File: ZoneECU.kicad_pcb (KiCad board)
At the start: 4 copper layers, 70.5 x 76.3 mm, 85 parts, among them J1 5007620481, J2 Conn_02x03_Odd_Even, SW1 SW_Push, U1 STM32F103RBTx, U2 SN65HVD234, U3 LMR50410, U4 LMR50410, U5 MAX3221, U7 DRV8871DDA, U9 SN74LVC4245A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

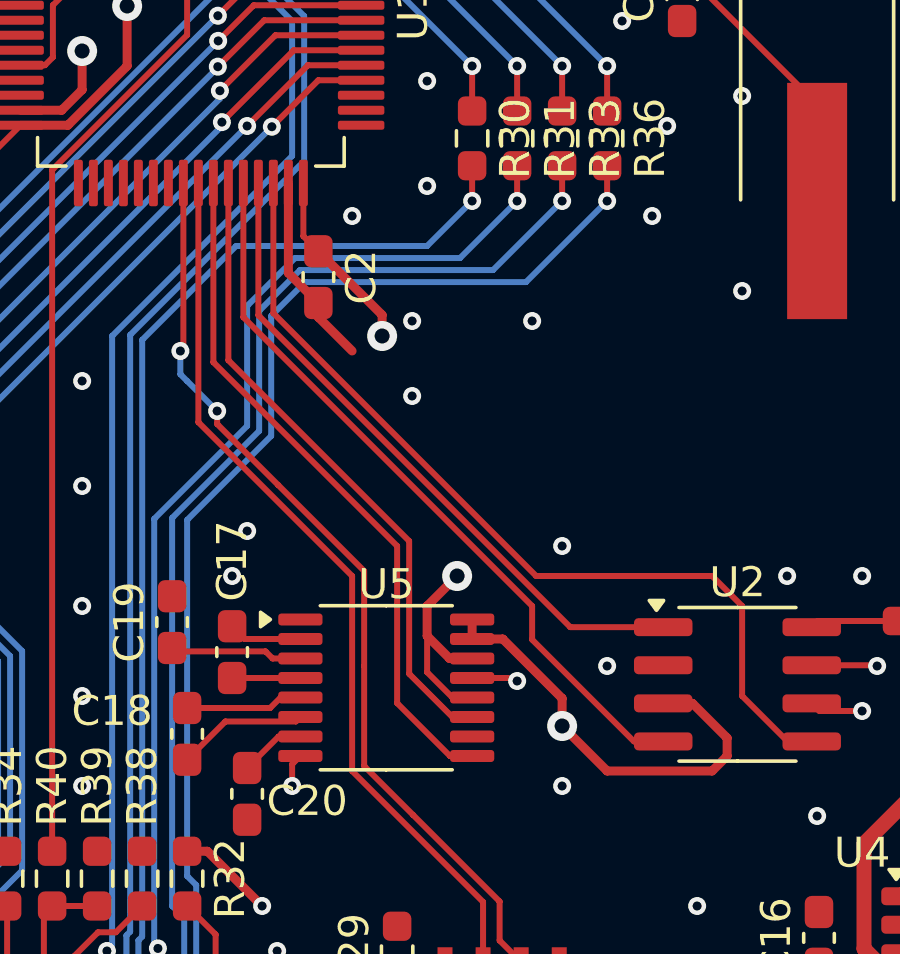
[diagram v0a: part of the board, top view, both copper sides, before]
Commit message: Swapped USART1 RX/TX, added pull ups for USART lines
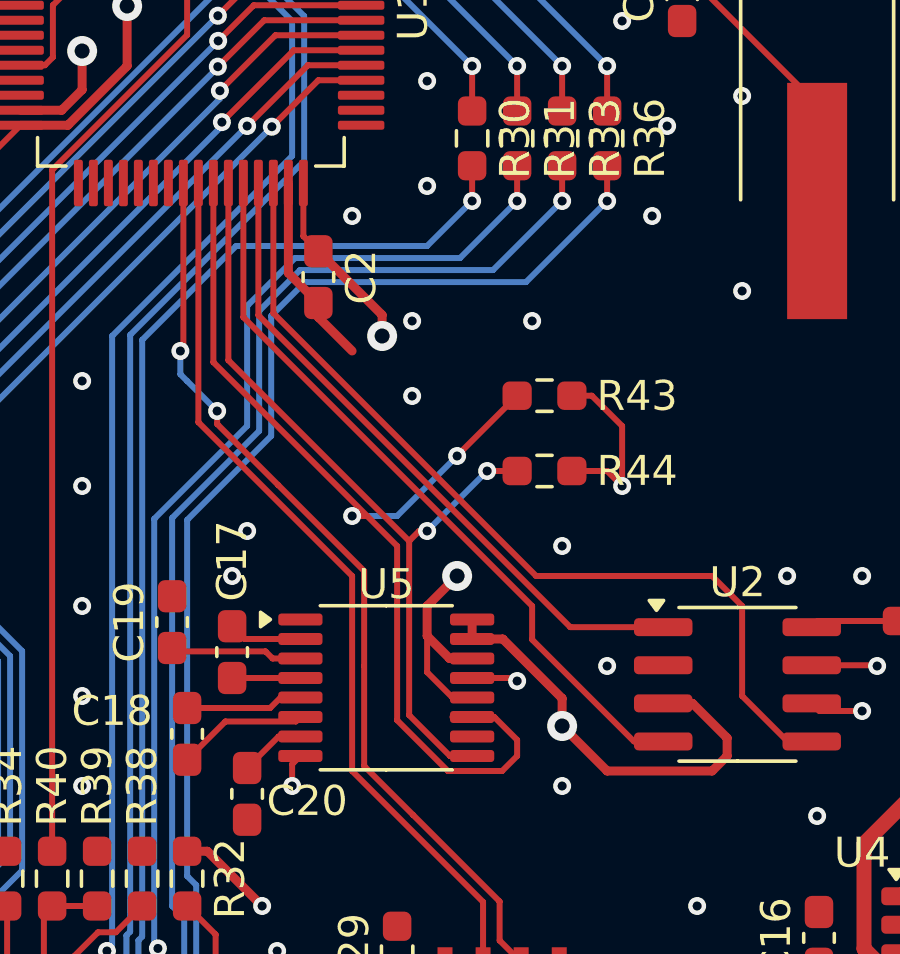
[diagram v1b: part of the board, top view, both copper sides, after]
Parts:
- added R43: 100k, Resistor_SMD:R_0603_1608Metric_Pad0.98x0.95mm_HandSolder, F.Cu at (143.4, 103.0)
- added R44: 100k, Resistor_SMD:R_0603_1608Metric_Pad0.98x0.95mm_HandSolder, F.Cu at (143.4, 105.5)
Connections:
- U1 pad 42: /USART1_RX -> /USART1_TX
- U1 pad 43: /USART1_TX -> /USART1_RX
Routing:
- net /3V3: track 269.2 -> 284.0 mm, vias 9 -> 10
- net /USART1_TX: track 21.6 -> 36.0 mm, vias 0 -> 2
- net /USART1_RX: track 23.1 -> 27.5 mm, vias 0 -> 2

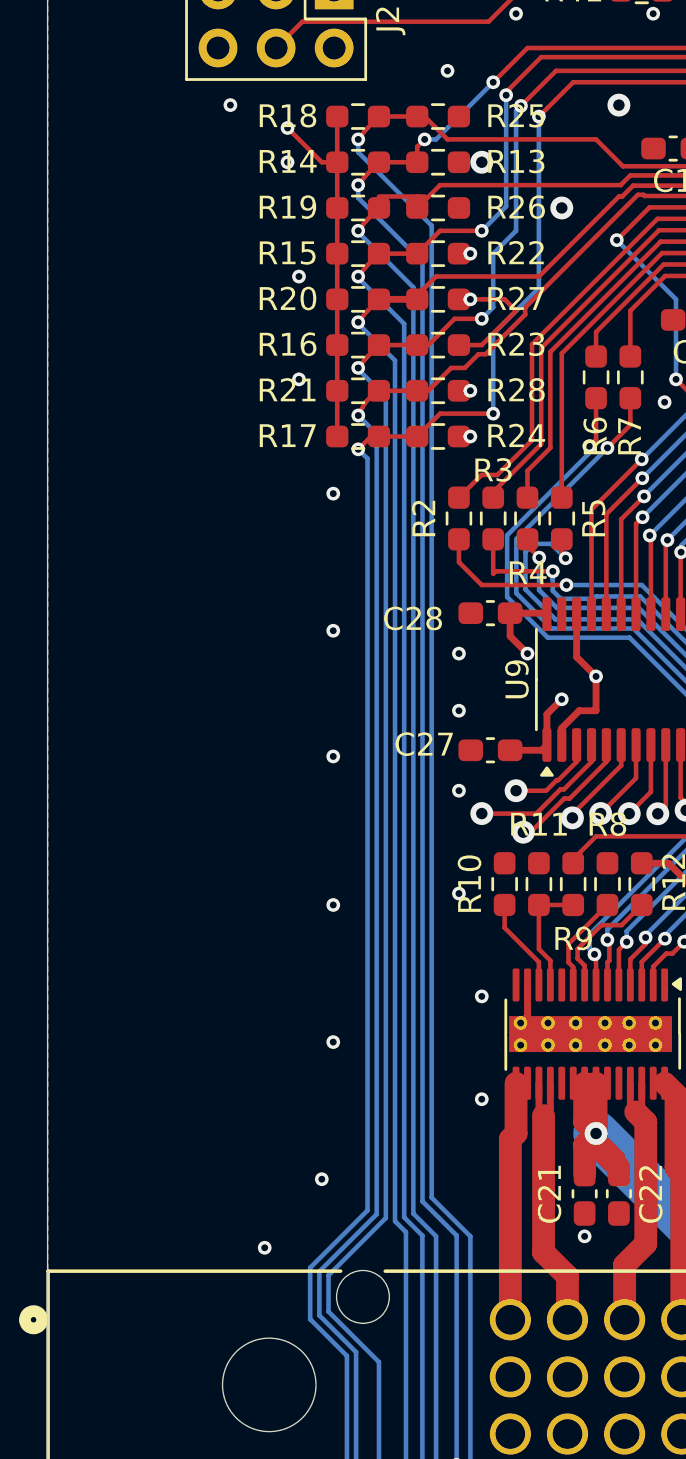
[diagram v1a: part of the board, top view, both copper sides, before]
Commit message: Add serial resistors on input pins
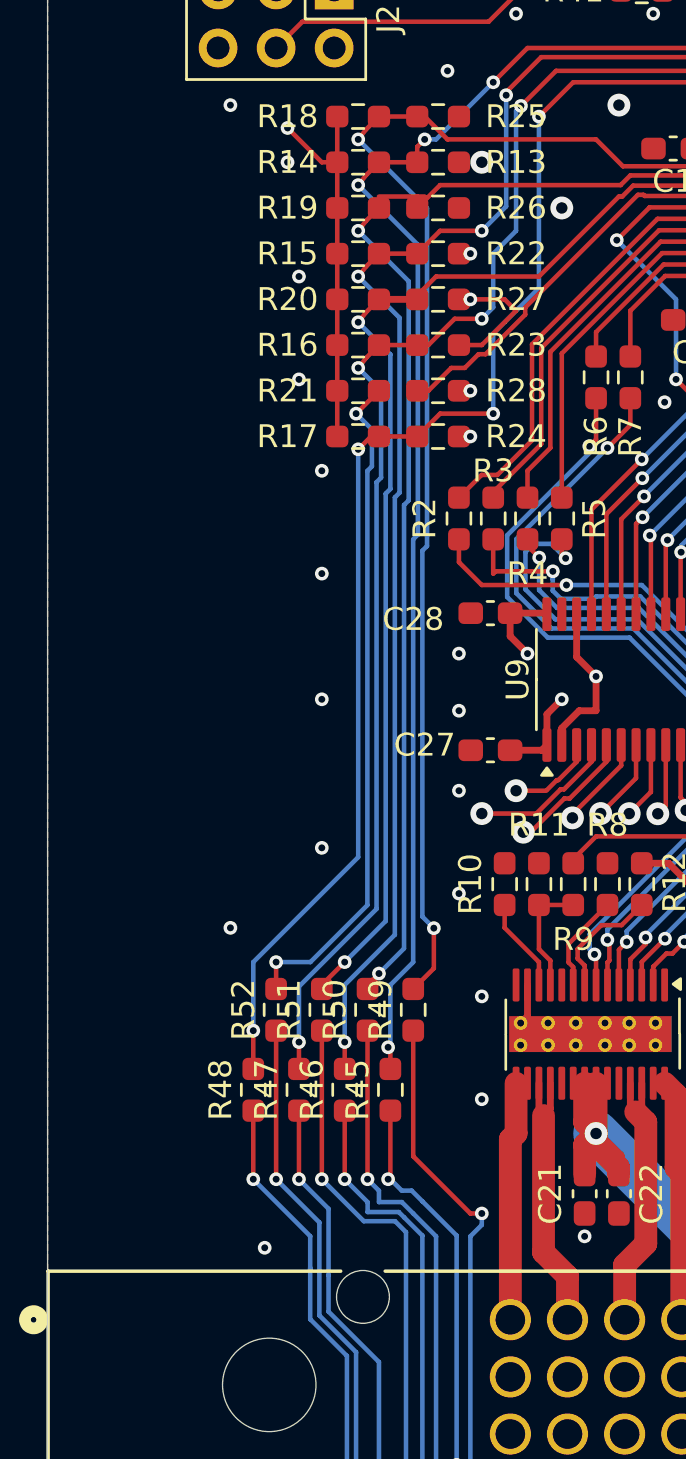
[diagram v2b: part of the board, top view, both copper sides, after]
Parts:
- added R45: NP, Resistor_SMD:R_0603_1608Metric_Pad0.98x0.95mm_HandSolder, F.Cu at (110.0, 128.6)
- added R46: NP, Resistor_SMD:R_0603_1608Metric_Pad0.98x0.95mm_HandSolder, F.Cu at (108.0, 128.6)
- added R47: NP, Resistor_SMD:R_0603_1608Metric_Pad0.98x0.95mm_HandSolder, F.Cu at (106.0, 128.6)
- added R48: NP, Resistor_SMD:R_0603_1608Metric_Pad0.98x0.95mm_HandSolder, F.Cu at (104.0, 128.6)
- added R49: NP, Resistor_SMD:R_0603_1608Metric_Pad0.98x0.95mm_HandSolder, F.Cu at (111.0, 125.1)
- added R50: NP, Resistor_SMD:R_0603_1608Metric_Pad0.98x0.95mm_HandSolder, F.Cu at (109.0, 125.1)
- added R51: NP, Resistor_SMD:R_0603_1608Metric_Pad0.98x0.95mm_HandSolder, F.Cu at (107.0, 125.1)
- added R52: NP, Resistor_SMD:R_0603_1608Metric_Pad0.98x0.95mm_HandSolder, F.Cu at (105.0, 125.1)
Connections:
- R13 pad 1: /IN1 -> /IN_MCU1
- R14 pad 2: /IN1 -> /IN_MCU1
- R15 pad 2: /IN2 -> /IN_MCU2
- R16 pad 2: /IN3 -> /IN_MCU3
- R17 pad 2: /IN4 -> /IN_MCU4
- R18 pad 2: /IN5 -> /IN_MCU5
- R19 pad 2: /IN6 -> /IN_MCU6
- R20 pad 2: /IN7 -> /IN_MCU7
- R21 pad 2: /IN8 -> /IN_MCU8
- R22 pad 1: /IN2 -> /IN_MCU2
- R23 pad 1: /IN3 -> /IN_MCU3
- R24 pad 1: /IN4 -> /IN_MCU4
- R25 pad 1: /IN5 -> /IN_MCU5
- R26 pad 1: /IN6 -> /IN_MCU6
- R27 pad 1: /IN7 -> /IN_MCU7
- R28 pad 1: /IN8 -> /IN_MCU8
- U1 pad 14: /IN1 -> /IN_MCU1
- U1 pad 15: /IN2 -> /IN_MCU2
- U1 pad 16: /IN3 -> /IN_MCU3
- U1 pad 17: /IN4 -> /IN_MCU4
- U1 pad 20: /IN5 -> /IN_MCU5
- U1 pad 21: /IN6 -> /IN_MCU6
- U1 pad 22: /IN7 -> /IN_MCU7
- U1 pad 23: /IN8 -> /IN_MCU8
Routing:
- net /IN1: track 85.1 -> 19.9 mm, vias 4 -> 2
- net /IN_MCU1: track 0.00 -> 64.9 mm, vias 0 -> 4
- net /IN_MCU2: track 0.00 -> 64.1 mm, vias 0 -> 4
- net /IN2: track 88.9 -> 25.8 mm, vias 4 -> 2
- net /IN3: track 93.3 -> 30.4 mm, vias 4 -> 2
- net /IN_MCU3: track 0.00 -> 62.0 mm, vias 0 -> 4
- net /IN_MCU4: track 0.00 -> 60.9 mm, vias 0 -> 4
- net /IN4: track 96.0 -> 35.1 mm, vias 4 -> 2
- net /IN5: track 93.8 -> 35.7 mm
- net /IN_MCU5: track 0.00 -> 57.9 mm, vias 0 -> 2
- net /IN_MCU6: track 0.00 -> 53.7 mm, vias 0 -> 2
- net /IN6: track 92.9 -> 39.5 mm
- net /IN_MCU7: track 0.00 -> 51.0 mm, vias 0 -> 2
- net /IN7: track 93.7 -> 44.1 mm
- net /IN8: track 97.4 -> 48.1 mm
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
